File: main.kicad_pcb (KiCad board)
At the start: 2 copper layers, 52.8 x 19.1 mm, 23 parts, among them J1 USB_OTG, J2 MCS-48 PINS, J3 SPI, J4 EXT2, J5 EXT1, SW1 SW_SPST, U1 LTC4415, U2 STF202-22, U5 AT90USB1286-AU, Y1 16Mhz

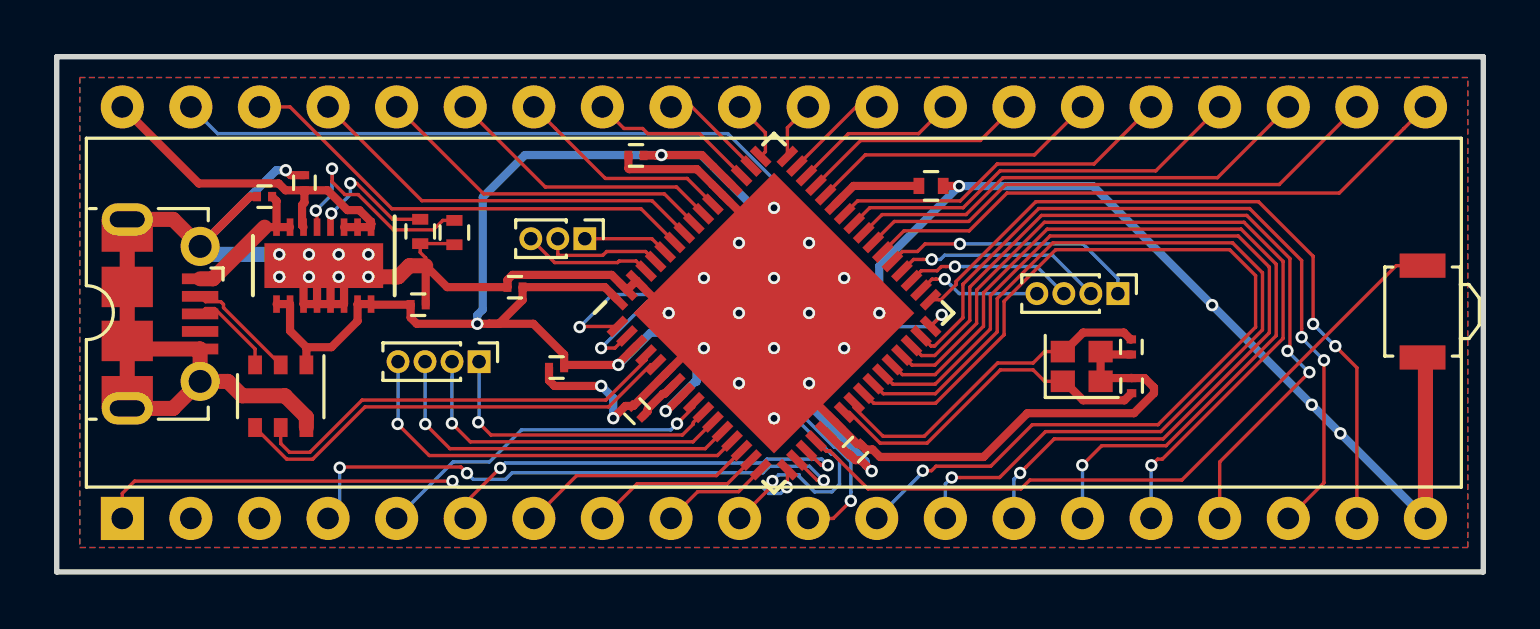
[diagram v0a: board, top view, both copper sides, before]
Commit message: cleaned up pcb, added status LEDs
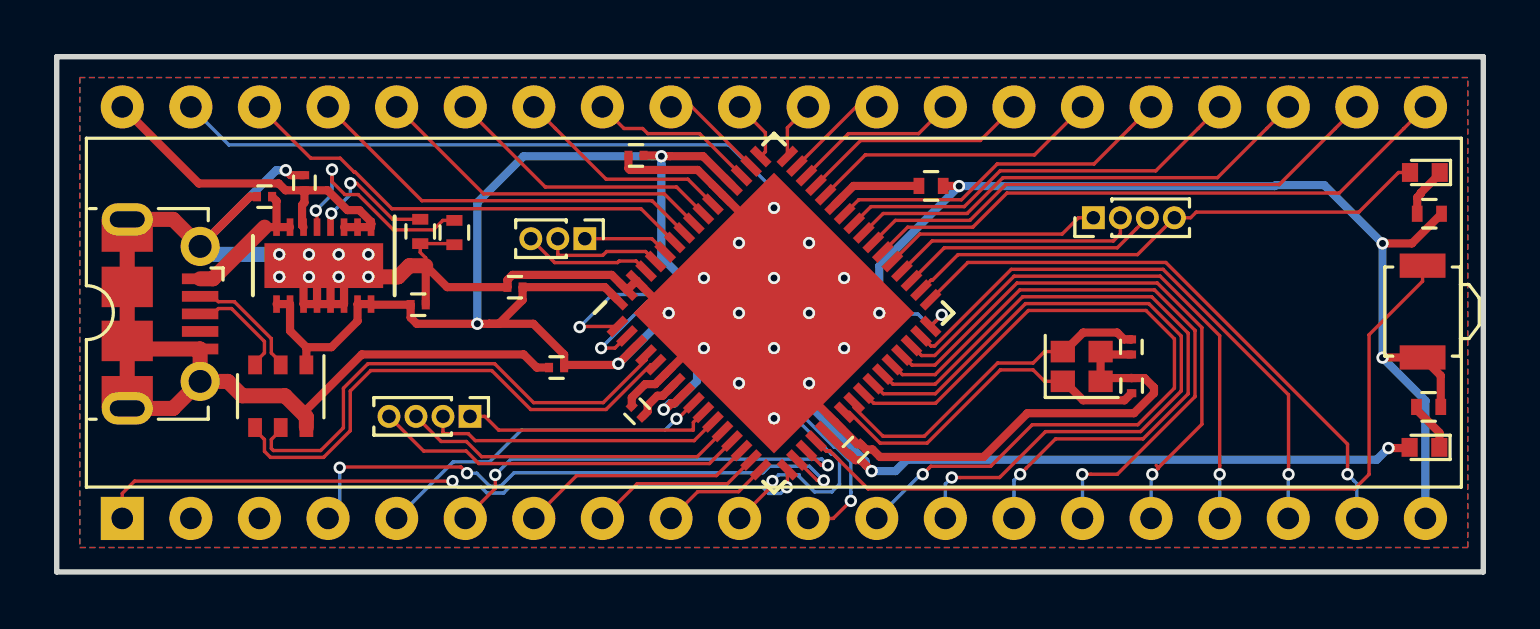
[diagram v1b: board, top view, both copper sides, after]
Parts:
- added D1: PWR, LEDs:LED_0402, F.Cu at (155.2, 103.9)
- added D2: PWR, LEDs:LED_0402, F.Cu at (155.2, 93.7)
- added R4: 250, Resistors_SMD:R_0402, F.Cu at (155.4, 102.4)
- added R5: 250, Resistors_SMD:R_0402, F.Cu at (155.4, 95.2)
- moved J5 2.95 mm to (143.0, 95.4), turned to 90 degrees
- moved J3 2.05 mm to (119.9, 102.7)
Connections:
- net Net-(J5-Pad4) renamed /ON
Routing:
- net +5VD: track 64.9 -> 84.6 mm, vias 5 -> 6
- net /ON: track 4.68 -> 19.9 mm, vias 1 -> 0
- net GNDD: track 158.7 -> 170.8 mm, vias 31 -> 28
- net /D3: track 31.7 -> 22.7 mm
- net /D2: track 33.5 -> 24.8 mm
- net /D0: track 37.1 -> 28.4 mm
- net /D1: track 35.6 -> 26.9 mm
- net /D5: track 29.1 -> 20.5 mm, vias 2 -> 1
- net /D4: track 29.4 -> 21.2 mm
- net /D6: track 28.3 -> 21.4 mm, vias 2 -> 1
- net /D7: track 27.0 -> 21.7 mm, vias 2 -> 1
- net Net-(J5-Pad3): track 6.27 -> 9.70 mm, vias 1 -> 0
- net Net-(SW1-Pad1): track 26.6 -> 30.0 mm
- net /D-: track 15.8 -> 18.5 mm
- net /D+: track 16.8 -> 19.1 mm
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
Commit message: legal shenanigans
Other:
- board text added: "Copyright Listofoptions (James M.) 2019. This documentation describes Open Hardware and is licensed under the CERN OHL v. 1.2. You may redistribute and modify this documentation under the terms of the CERN OHL v.1.2. (http://ohwr.org/cernohl). This documentation is distributed WITHOUT ANY EXPRESS OR IMPLIED WARRANTY,INCLUDING OF MERCHANTABILITY, SATISFACTORY QUALITY AND FITNESS FOR A PARTICULAR P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"
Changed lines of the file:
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@@
 (kicad_pcb (version 4) (host pcbnew 4.0.7)
   (general
-    (links 147)
+    (links 129)
     (no_connects 0)
     (area 104.476874 89.318422 157.506876 108.598424)
     (thickness 1.6)
-    (drawings 4)
+    (drawings 5)
     (tracks 704)
     (zones 0)
@@
     (39 F.Mask user)
     (40 Dwgs.User user hide)
-    (41 Cmts.User user hide)
+    (41 Cmts.User user)
     (42 Eco1.User user hide)
     (43 Eco2.User user)
@@
     )
   )
+  (gr_text "Copyright Listofoptions (James M.) 2019.\nThis documentation describes Open Hardware and is licensed under the\nCERN OHL v. 1.2. You may redistribute and modify this documentation under the\nterms of the CERN OHL v.1.2. (http://ohwr.org/cernohl). This documentation is\ndistributed WITHOUT ANY EXPRESS OR IMPLIED WARRANTY,INCLUDING OF\nMERCHANTABILITY, SATISFACTORY QUALITY AND FITNESS FOR A PARTICULAR PURPOSE.\nPlease see the CERN OHL v.1.2 for applicable conditions" (at 12.12596 189.26048) (layer Cmts.User)
+    (effects (font (size 1.5 1.5) (thickness 0.3)) (justify left))
+  )
   (gr_line (start 157.406875 89.418423) (end 104.576875 89.418423) (layer Edge.Cuts) (width 0.2))
   (gr_line (start 157.406875 108.498423) (end 157.406875 89.418423) (layer Edge.Cuts) (width 0.2))
   (gr_line (start 104.576875 108.498423) (end 157.406875 108.498423) (layer Edge.Cuts) (width 0.2))
   (gr_line (start 104.576875 108.498423) (end 104.576875 89.418423) (layer Edge.Cuts) (width 0.2))
+  (segment (start 130.79273 97.331428) (end 130.79273 97.314288) (width 0.127) (layer F.Cu) (net 0) (status 30))
   (segment (start 113.217635 95.729783) (end 112.717635 95.729783) (width 0.3048) (layer F.Cu) (net 1) (status 30))
   (segment (start 112.717635 95.729783) (end 112.717635 94.764103) (width 0.3048) (layer F.Cu) (net 1) (status 10))
@@
   (segment (start 109.888515 97.642943) (end 110.363515 97.642943) (width 0.5588) (layer F.Cu) (net 1) (status 30))
   (segment (start 110.363515 97.642943) (end 112.276675 95.729783) (width 0.5588) (layer F.Cu) (net 1) (status 10))
-  (segment (start 130.79273 97.331428) (end 130.79273 97.314288) (width 0.127) (layer F.Cu) (net 2) (status 30))
   (segment (start 155.265115 102.153715) (end 155.265115 105.385853) (width 0.3048) (layer B.Cu) (net 2))
   (segment (start 155.265115 105.385853) (end 155.265115 106.517223) (width 0.3048) (layer B.Cu) (net 2))

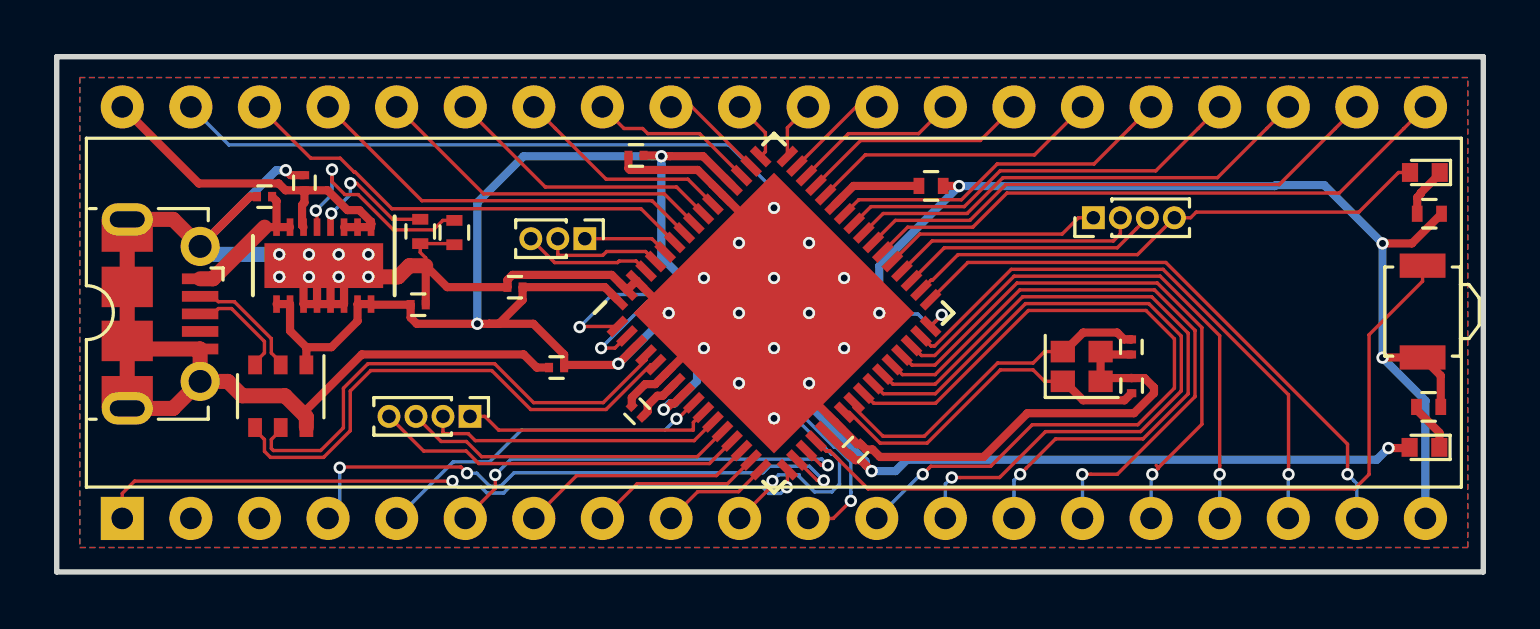
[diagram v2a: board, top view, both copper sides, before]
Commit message: improved groundplane, and used beefier supply caps
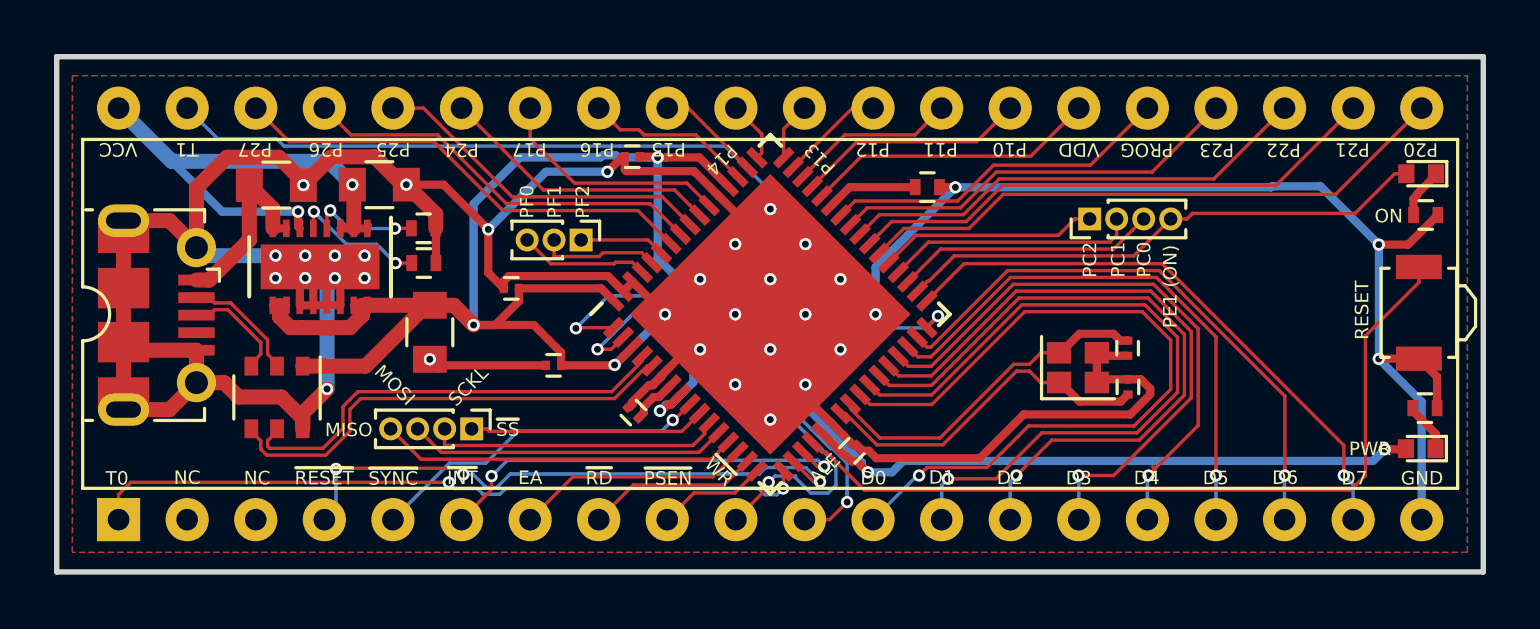
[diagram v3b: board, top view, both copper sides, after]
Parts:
- C10, C8, C9: value 4u7 -> 100u; footprint Capacitors_SMD:C_0201 -> Capacitors_SMD:C_0805
- moved C9 2.77 mm to (116.5, 94.2), turned to 0 degrees
- moved R3 1.60 mm to (118.2, 97.1), turned to 180 degrees
- moved C10 1.11 mm to (118.4, 99.6), turned to 270 degrees
- moved C8 0.61 mm to (112.7, 94.2), turned to 0 degrees
- moved J3 0.47 mm to (119.9, 103.2)
- moved R2 0.17 mm to (118.2, 95.8), turned to 180 degrees
- moved R5 0.14 mm to (155.3, 95.3)
- moved Y1 0.14 mm to (142.4, 100.9)
- moved J1 0.14 mm to (107.4, 99.0)
- moved J2 0.14 mm to (106.9, 106.6)
- moved U2 0.14 mm to (112.7, 102.0)
- moved C1 0.14 mm to (125.9, 93.1)
- moved C3 0.14 mm to (144.2, 101.6)
- moved C4 0.14 mm to (125.9, 102.6)
- moved C5 0.14 mm to (134.0, 104.0)
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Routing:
- net GNDD: track 170.7 -> 181.2 mm, vias 28 -> 33
- net VCC: track 13.8 -> 18.7 mm, vias 0 -> 2
- net +5VD: track 84.6 -> 89.4 mm
- net Net-(R3-Pad2): track 8.27 -> 5.04 mm
- net /D-: track 18.5 -> 16.7 mm
- net /D+: track 19.1 -> 17.3 mm
- net VBUS: track 5.32 -> 7.07 mm
- net Net-(R2-Pad2): track 5.07 -> 4.01 mm
- net /P17: track 8.13 -> 8.79 mm
- net /MISO: track 13.8 -> 13.2 mm
- net /MOSI: track 12.4 -> 11.8 mm
- net /~SS: track 9.29 -> 8.75 mm
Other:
- board text added: "ALE"
- board text added: "D0"
- board text added: "D1"
- board text added: "D2"
- board text added: "D3"
- board text added: "D4"
- board text added: "D5"
- board text added: "D6"
- board text added: "D7"
- board text added: "EA"
- board text added: "GND"
- board text added: "MISO"
- board text added: "MOSI"
- board text added: "NC"
- board text added: "ON"
- board text added: "P10"
- board text added: "P11"
- board text added: "P12"
- board text added: "P13"
- board text added: "P14"
- board text added: "P15"
- board text added: "P16"
- board text added: "P17"
- board text added: "P20"
- board text added: "P21"
- board text added: "P22"
- board text added: "P23"
- board text added: "P24"
- board text added: "P25"
- board text added: "P26"
- board text added: "P27"
- board text added: "PC0"
- board text added: "PC1"
- board text added: "PC2"
- board text added: "PE1 (ON)"
- board text added: "PF0"
- board text added: "PF1"
- board text added: "PF2"
- board text added: "PROG"
- board text added: "PWR"
- board text added: "RESET"
- board text added: "SCKL"
- board text added: "T0"
- board text added: "T1"
- board text added: "VCC"
- board text added: "VDD"
- board text added: "~INT"
- board text added: "~PSEN"
- board text added: "~RD"
- board text added: "~RESET"
- board text added: "~SS"
- board text added: "~SYNC"
- board text added: "~WR"

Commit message: shenanigans and bootloader jumper on clock xtal-1 pin
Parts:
- added JP1: BOOT, Resistors_SMD:R_0201_NoSilk, F.Cu at (136.4, 103.1)
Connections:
- C2 pad 2: /XTAL+ -> Net-(C2-Pad2)
- Y1 pad 4: /XTAL+ -> Net-(C2-Pad2)
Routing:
- net /XTAL+: track 12.6 -> 2.75 mm
- net Net-(C2-Pad2): track 0.00 -> 9.23 mm
- net VCC: track 18.7 -> 15.9 mm
- net +5VD: track 89.4 -> 91.6 mm
- net /~RESET: track 22.1 -> 21.1 mm, vias 3 -> 2
- net /T0: track 26.8 -> 27.5 mm, vias 2 -> 3
- net /~WR: track 18.9 -> 18.4 mm
- net /~INT: track 15.7 -> 15.5 mm, vias 2 -> 1
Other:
- board text added: "BOOT"
